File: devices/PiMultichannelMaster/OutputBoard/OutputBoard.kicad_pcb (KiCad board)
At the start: 2 copper layers, 88.3 x 48.3 mm, 69 parts, among them J1 RJ45-2x4Port, P1 CONN_02X15, Q1 2N7002, Q10 2N7002, Q11 2N7002, Q12 2N7002, Q13 BSS84, Q14 BSS84, Q15 BSS84, Q16 BSS84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

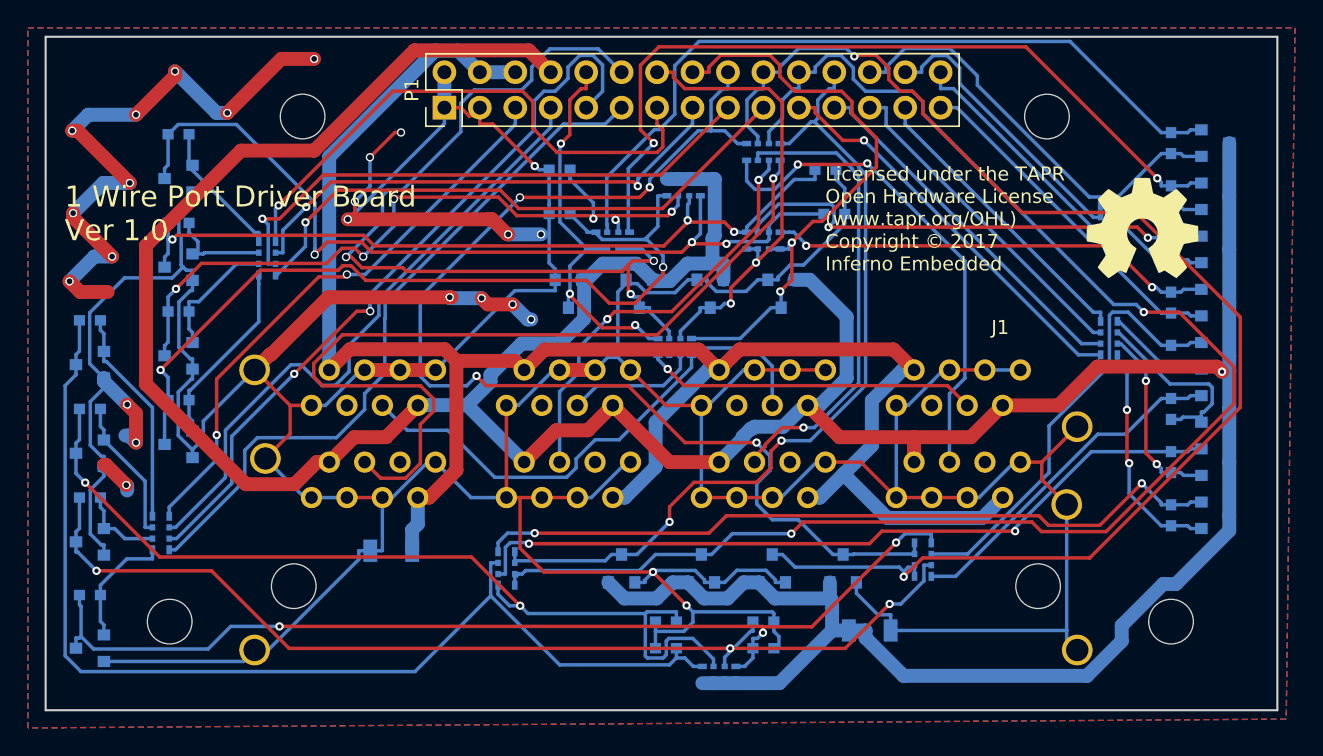
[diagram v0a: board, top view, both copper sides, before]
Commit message: Add pullups to the PiMultichannelMaster outputboard pullup mosfet
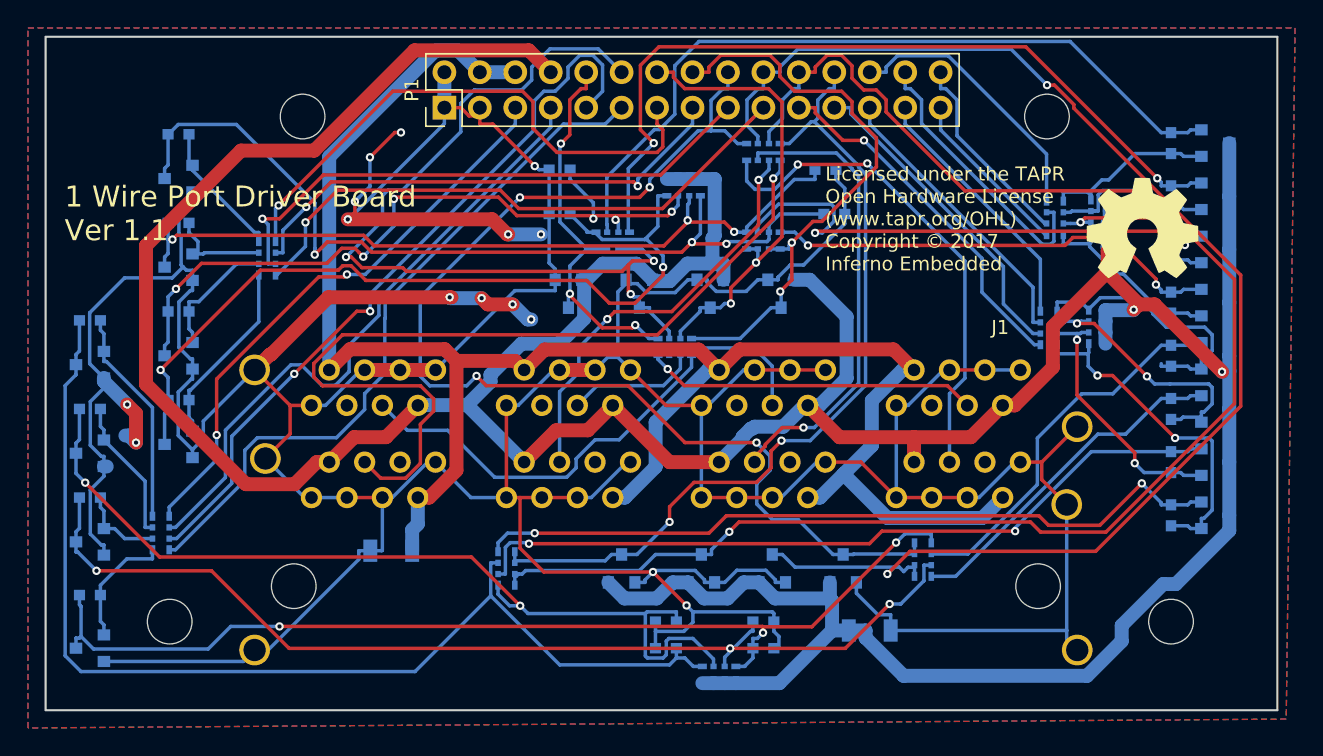
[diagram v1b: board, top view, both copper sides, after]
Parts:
- added RP13: 100k, 0603-pack4:0603_Pack4, B.Cu at (204.3, 98.3)
- added RP14: 100k, 0603-pack4:0603_Pack4, B.Cu at (204.4, 90.4)
- moved RP2 4.38 mm to (200.8, 98.3)
- moved RP8 3.89 mm to (201.2, 90.4)
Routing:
- net (no net): track 46.5 -> 0.00 mm, vias 10 -> 0
- net +5V: track 284.9 -> 302.8 mm, vias 1 -> 3
- net Net-(C10-Pad2): track 7.55 -> 19.6 mm
- net Net-(C7-Pad2): track 16.5 -> 24.6 mm
- net Net-(C20-Pad2): track 7.04 -> 13.8 mm, vias 0 -> 2
- net Net-(C9-Pad2): track 13.6 -> 19.4 mm, vias 0 -> 2
- net Net-(C21-Pad2): track 6.42 -> 11.8 mm
- net Net-(C8-Pad2): track 13.6 -> 18.4 mm
- net /Driver1/PU1: track 35.4 -> 39.9 mm
- net Net-(C22-Pad2): track 8.04 -> 12.5 mm
- net Net-(C19-Pad2): track 9.53 -> 13.6 mm
- net /Driver0/PU3: track 31.7 -> 27.6 mm
- net /SENSE1: track 109.1 -> 113.1 mm, vias 2 -> 1
- net /DPU7: track 22.9 -> 19.7 mm
- net /DPU2: track 24.0 -> 20.8 mm
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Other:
- board text added: "1 Wire Port Driver Board Ver 1.1"
- board text removed: "1 Wire Port Driver Board Ver 1.0"
